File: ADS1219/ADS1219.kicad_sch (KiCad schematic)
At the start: 19 parts, among them J1 qwiic, J2 Conn_01x06, J3 qwiic, J4 DRDY, U1 ADS1219IPW, U2 NCP51460SN33T1G

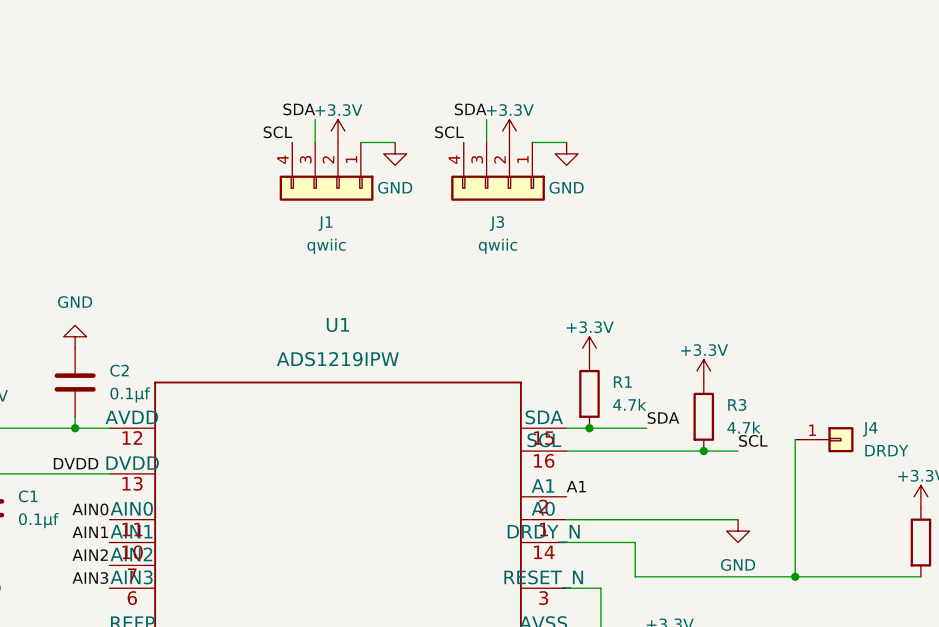
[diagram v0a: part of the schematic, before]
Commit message: Cleaning up ADS1219 board folders
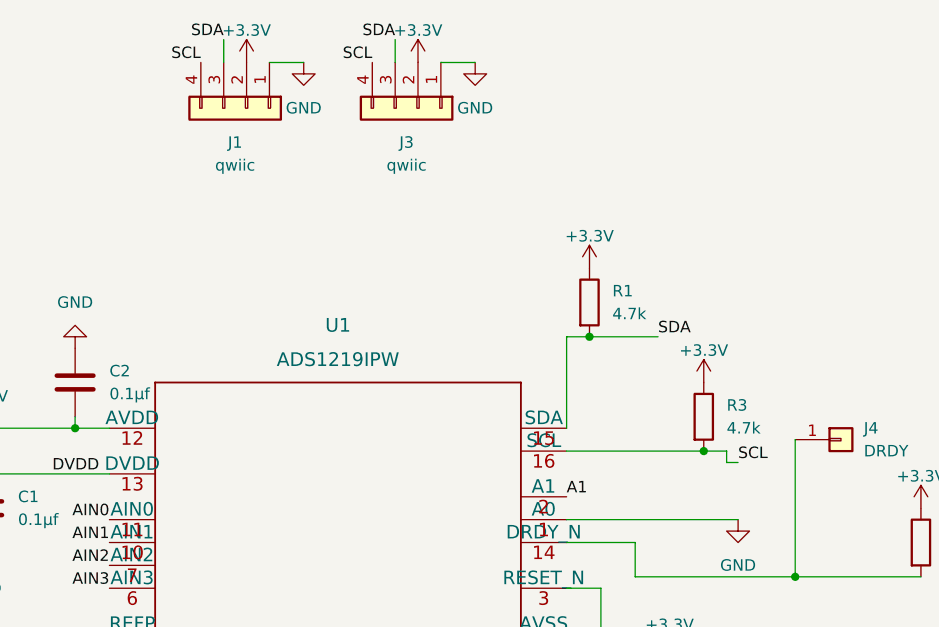
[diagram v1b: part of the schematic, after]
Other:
- moved on the sheet: J1, J3, R1

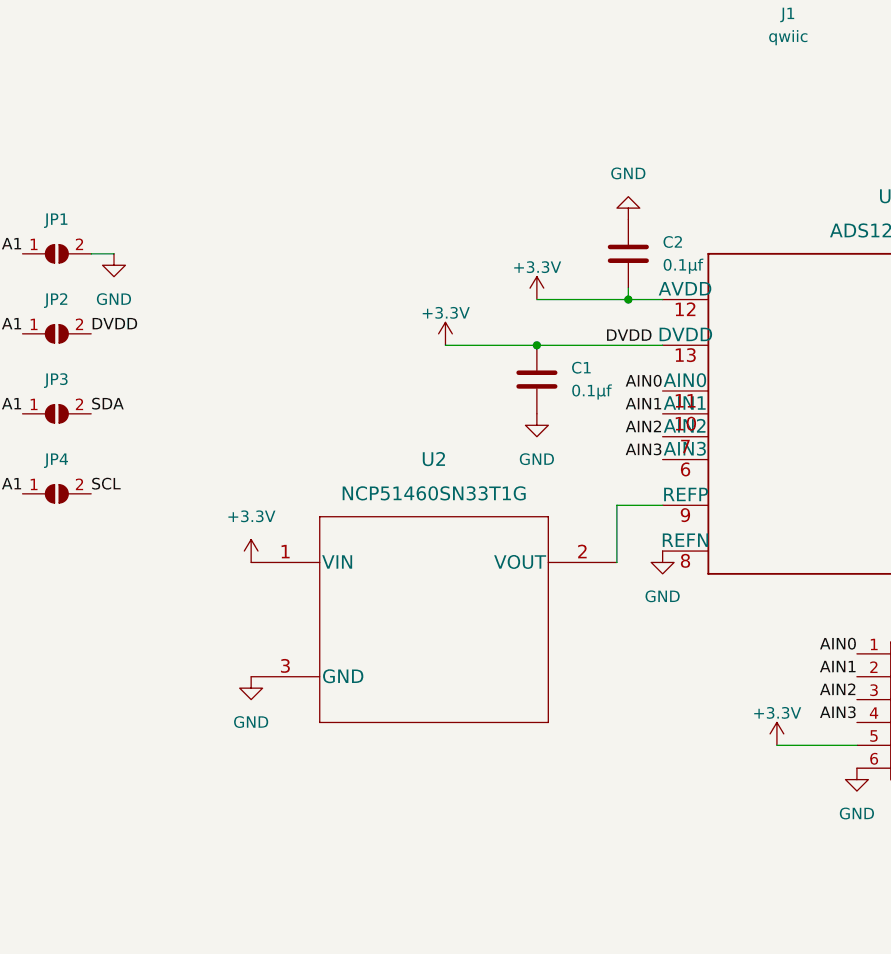
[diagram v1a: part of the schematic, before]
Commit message: add C3, 0.1uF decoupling cap for voltage reference IC - also rework board text labels
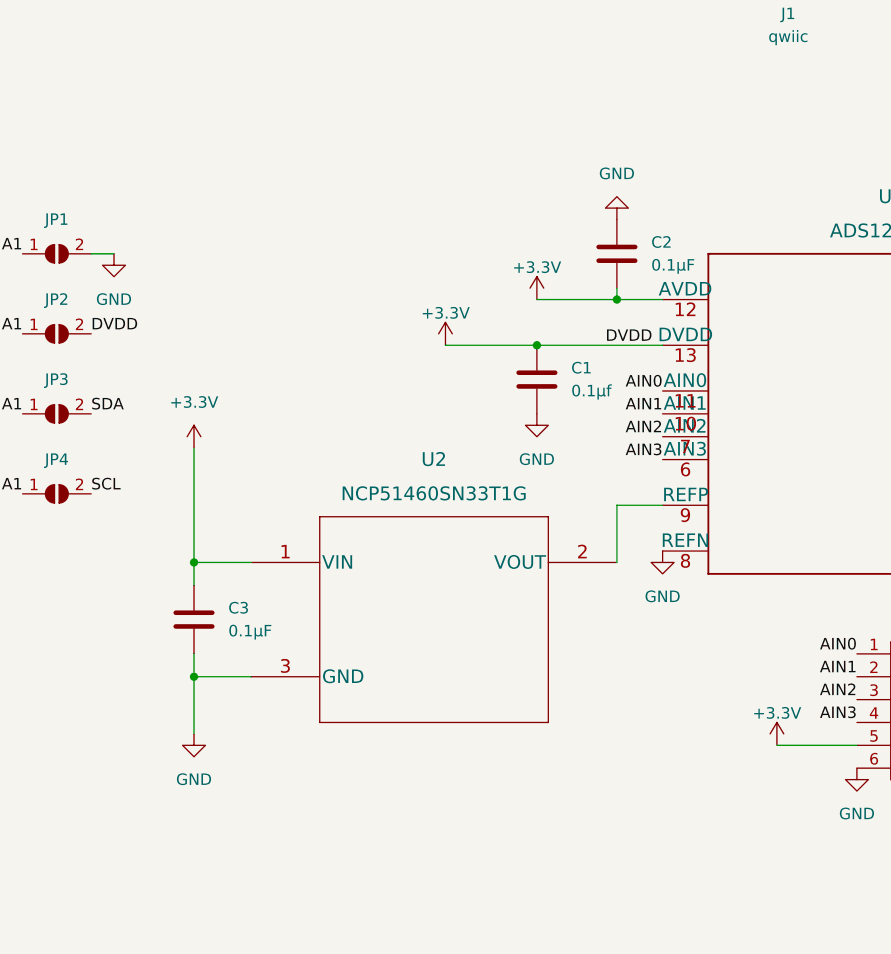
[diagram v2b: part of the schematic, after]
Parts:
- added C3: 0.1μF, Capacitor_SMD:C_0805_2012Metric_Pad1.18x1.45mm_HandSolder, symbol Device:C
- C2: value 0.1μf -> 0.1μF
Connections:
- net +3.3V: now also C3.1
- net GND: now also C3.2
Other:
- moved on the sheet: C2
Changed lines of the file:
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@@
   (junction (at 162.56 54.61) (diameter 0) (color 0 0 0 0)
   )
-  (junction (at 105.41 64.77) (diameter 0) (color 0 0 0 0)
+  (junction (at 57.15 106.68) (diameter 0) (color 0 0 0 0)
   )
   (junction (at 160.02 92.71) (diameter 0) (color 0 0 0 0)
   )
+  (junction (at 57.15 93.98) (diameter 0) (color 0 0 0 0)
+  )
+  (junction (at 104.14 64.77) (diameter 0) (color 0 0 0 0)
+  )
   (junction (at 95.25 69.85) (diameter 0) (color 0 0 0 0)
   )
@@
     (stroke (width 0) (type default))
   )
-  (wire (pts (xy 105.41 64.77) (xy 109.22 64.77))
+  (wire (pts (xy 57.15 81.28) (xy 57.15 93.98))
     (stroke (width 0) (type default))
   )
@@
     (stroke (width 0) (type default))
   )
+  (wire (pts (xy 57.15 93.98) (xy 63.5 93.98))
+    (stroke (width 0) (type default))
+  )
   (wire (pts (xy 160.02 54.61) (xy 160.02 64.77))
     (stroke (width 0) (type default))
@@
     (stroke (width 0) (type default))
   )
-  (wire (pts (xy 95.25 64.77) (xy 105.41 64.77))
+  (wire (pts (xy 95.25 64.77) (xy 104.14 64.77))
     (stroke (width 0) (type default))
   )
@@
     (stroke (width 0) (type default))
   )
+  (wire (pts (xy 57.15 106.68) (xy 57.15 113.03))
+    (stroke (width 0) (type default))
+  )
   (wire (pts (xy 130.81 24.13) (xy 127 24.13))
     (stroke (width 0) (type default))
   )
+  (wire (pts (xy 57.15 93.98) (xy 57.15 96.52))
+    (stroke (width 0) (type default))
+  )
   (wire (pts (xy 104.14 87.63) (xy 109.22 87.63))
     (stroke (width 0) (type default))
   )
+  (wire (pts (xy 104.14 64.77) (xy 109.22 64.77))
+    (stroke (width 0) (type default))
+  )
   (wire (pts (xy 162.56 54.61) (xy 160.02 54.61))
     (stroke (width 0) (type default))
   )
+  (wire (pts (xy 57.15 104.14) (xy 57.15 106.68))
+    (stroke (width 0) (type default))
+  )
   (wire (pts (xy 121.92 114.3) (xy 130.81 114.3))
     (stroke (width 0) (type default))
   )
-  (wire (pts (xy 105.41 63.5) (xy 105.41 64.77))
+  (wire (pts (xy 104.14 63.5) (xy 104.14 64.77))
     (stroke (width 0) (type default))
   )
@@
   )
   (wire (pts (xy 160.02 87.63) (xy 160.02 92.71))
+    (stroke (width 0) (type default))
+  )
+  (wire (pts (xy 57.15 106.68) (xy 63.5 106.68))
     (stroke (width 0) (type default))
   )
@@
     )
   )
+  (symbol (lib_id "power:GND") (at 57.15 113.03 0) (unit 1)
+    (in_bom yes) (on_board yes) (dnp no) (fields_autoplaced)
+    (property "Reference" "#PWR03" (at 57.15 119.38 0)
+      (effects (font (size 1.27 1.27)) hide)
+    )
+    (property "Value" "GND" (at 57.15 118.11 0)
+      (effects (font (size 1.27 1.27)))
+    )
+    (property "Footprint" "" (at 57.15 113.03 0)
+      (effects (font (size 1.27 1.27)) hide)
+    )
+    (property "Datasheet" "" (at 57.15 113.03 0)
+      (effects (font (size 1.27 1.27)) hide)
+    )
+    (pin "1")
+    (instances
+      (project "ADS1219"
+        (path "/7e530dfb-4b7f-4624-94df-744a2f909c74"
+          (reference "#PWR03") (unit 1)
+        )
+      )
+    )
+  )
   (symbol (lib_id "Mechanical:MountingHole") (at 219.71 22.86 0) (unit 1)
     (in_bom yes) (on_board yes) (dnp no) (fields_autoplaced)
@@
     )
   )
-  (symbol (lib_id "power:GND") (at 63.5 106.68 0) (unit 1)
-    (in_bom yes) (on_board yes) (dnp no) (fields_autoplaced)
-    (property "Reference" "#PWR0113" (at 63.5 113.03 0)
-      (effects (font (size 1.27 1.27)) hide)
-    )
-    (property "Value" "GND" (at 63.5 111.76 0)
-      (effects (font (size 1.27 1.27)))
-    )
-    (property "Footprint" "" (at 63.5 106.68 0)
-      (effects (font (size 1.27 1.27)) hide)
-    )
-    (property "Datasheet" "" (at 63.5 106.68 0)
-      (effects (font (size 1.27 1.27)) hide)
-    )
-    (pin "1")
-    (instances
-      (project "ADS1219"
-        (path "/7e530dfb-4b7f-4624-94df-744a2f909c74"
-          (reference "#PWR0113") (unit 1)
-        )
-      )
-    )
-  )
   (symbol (lib_id "power:+3.3V") (at 124.46 24.13 0) (unit 1)
     (in_bom yes) (on_board yes) (dnp no) (fields_autoplaced)
@@
     )
   )
-  (symbol (lib_id "power:+3.3V") (at 63.5 93.98 0) (unit 1)
-    (in_bom yes) (on_board yes) (dnp no) (fields_autoplaced)
-    (property "Reference" "#PWR0111" (at 63.5 97.79 0)
-      (effects (font (size 1.27 1.27)) hide)
-    )
-    (property "Value" "+3.3V" (at 63.5 88.9 0)
-      (effects (font (size 1.27 1.27)))
-    )
-    (property "Footprint" "" (at 63.5 93.98 0)
-      (effects (font (size 1.27 1.27)) hide)
-    )
-    (property "Datasheet" "" (at 63.5 93.98 0)
-      (effects (font (size 1.27 1.27)) hide)
-    )
-    (pin "1")
-    (instances
-      (project "ADS1219"
-        (path "/7e530dfb-4b7f-4624-94df-744a2f909c74"
-          (reference "#PWR0111") (unit 1)
-        )
-      )
-    )
-  )
-  (symbol (lib_id "Device:C") (at 105.41 59.69 180) (unit 1)
-    (in_bom yes) (on_board yes) (dnp no) (fields_autoplaced)
-    (property "Reference" "C2" (at 109.22 58.4199 0)
+  (symbol (lib_id "Device:C") (at 104.14 59.69 180) (unit 1)
+    (in_bom yes) (on_board yes) (dnp no) (fields_autoplaced)
+    (property "Reference" "C2" (at 107.95 58.42 0)
       (effects (font (size 1.27 1.27)) (justify right))
     )
-    (property "Value" "0.1μf" (at 109.22 60.9599 0)
+    (property "Value" "0.1μF" (at 107.95 60.96 0)
       (effects (font (size 1.27 1.27)) (justify right))
     )
-    (property "Footprint" "Capacitor_SMD:C_0805_2012Metric_Pad1.18x1.45mm_HandSolder" (at 104.4448 55.88 0)
-      (effects (font (size 1.27 1.27)) hide)
-    )
-    (property "Datasheet" "~" (at 105.41 59.69 0)
+    (property "Footprint" "Capacitor_SMD:C_0805_2012Metric_Pad1.18x1.45mm_HandSolder" (at 103.1748 55.88 0)
+      (effects (font (size 1.27 1.27)) hide)
+    )
+    (property "Datasheet" "~" (at 104.14 59.69 0)
       (effects (font (size 1.27 1.27)) hide)
     )
@@
     )
   )
-  (symbol (lib_id "power:GND") (at 105.41 55.88 180) (unit 1)
-    (in_bom yes) (on_board yes) (dnp no) (fields_autoplaced)
-    (property "Reference" "#PWR010" (at 105.41 49.53 0)
-      (effects (font (size 1.27 1.27)) hide)
-    )
-    (property "Value" "GND" (at 105.41 50.8 0)
-      (effects (font (size 1.27 1.27)))
-    )
-    (property "Footprint" "" (at 105.41 55.88 0)
-      (effects (font (size 1.27 1.27)) hide)
-    )
-    (property "Datasheet" "" (at 105.41 55.88 0)
+  (symbol (lib_id "power:GND") (at 104.14 55.88 180) (unit 1)
+    (in_bom yes) (on_board yes) (dnp no) (fields_autoplaced)
+    (property "Reference" "#PWR010" (at 104.14 49.53 0)
+      (effects (font (size 1.27 1.27)) hide)
+    )
+    (property "Value" "GND" (at 104.14 50.8 0)
+      (effects (font (size 1.27 1.27)))
+    )
+    (property "Footprint" "" (at 104.14 55.88 0)
+      (effects (font (size 1.27 1.27)) hide)
+    )
+    (property "Datasheet" "" (at 104.14 55.88 0)
       (effects (font (size 1.27 1.27)) hide)
     )
@@
     )
   )
+  (symbol (lib_id "Device:C") (at 57.15 100.33 0) (unit 1)
+    (in_bom yes) (on_board yes) (dnp no) (fields_autoplaced)
+    (property "Reference" "C3" (at 60.96 99.06 0)
+      (effects (font (size 1.27 1.27)) (justify left))
+    )
+    (property "Value" "0.1μF" (at 60.96 101.6 0)
+      (effects (font (size 1.27 1.27)) (justify left))
+    )
+    (property "Footprint" "Capacitor_SMD:C_0805_2012Metric_Pad1.18x1.45mm_HandSolder" (at 58.1152 104.14 0)
+      (effects (font (size 1.27 1.27)) hide)
+    )
+    (property "Datasheet" "~" (at 57.15 100.33 0)
+      (effects (font (size 1.27 1.27)) hide)
+    )
+    (pin "1")
+    (pin "2")
+    (instances
+      (project "ADS1219"
+        (path "/7e530dfb-4b7f-4624-94df-744a2f909c74"
+          (reference "C3") (unit 1)
+        )
+      )
+    )
+  )
   (symbol (lib_id "power:GND") (at 48.26 59.69 0) (unit 1)
     (in_bom yes) (on_board yes) (dnp no) (fields_autoplaced)
@@
         )
       )
+    )
+  )
+  (symbol (lib_id "power:+3.3V") (at 57.15 81.28 0) (unit 1)
+    (in_bom yes) (on_board yes) (dnp no) (fields_autoplaced)
+    (property "Reference" "#PWR02" (at 57.15 85.09 0)
+      (effects (font (size 1.27 1.27)) hide)
+    )
+    (property "Value" "+3.3V" (at 57.15 76.2 0)
+      (effects (font (size 1.27 1.27)))
+    )
+    (property "Footprint" "" (at 57.15 81.28 0)
+      (effects (font (size 1.27 1.27)) hide)
+    )
+    (property "Datasheet" "" (at 57.15 81.28 0)
+      (effects (font (size 1.27 1.27)) hide)
+    )
+    (pin "1")
+    (instances
+      (project "ADS1219"
+        (path "/7e530dfb-4b7f-4624-94df-744a2f909c74"
+          (reference "#PWR02") (unit 1)
+        )
+      )
